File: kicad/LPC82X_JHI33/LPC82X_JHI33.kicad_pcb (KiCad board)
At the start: 2 copper layers, 2 parts

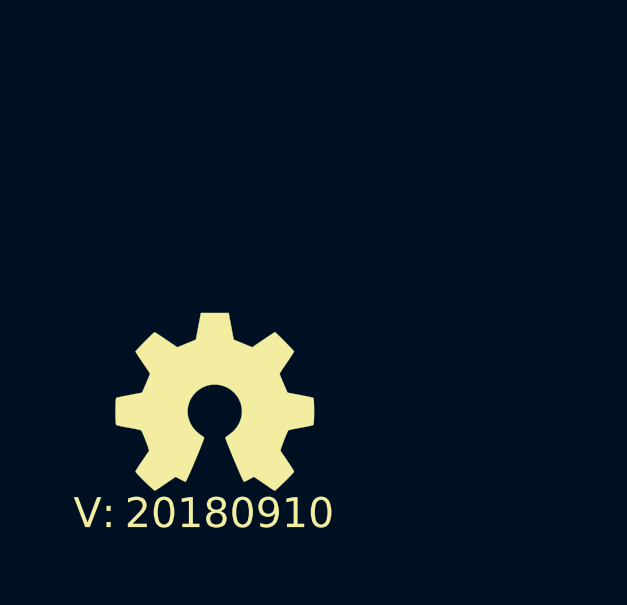
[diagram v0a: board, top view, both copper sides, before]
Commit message: started on LPC824 QFN33 breakout
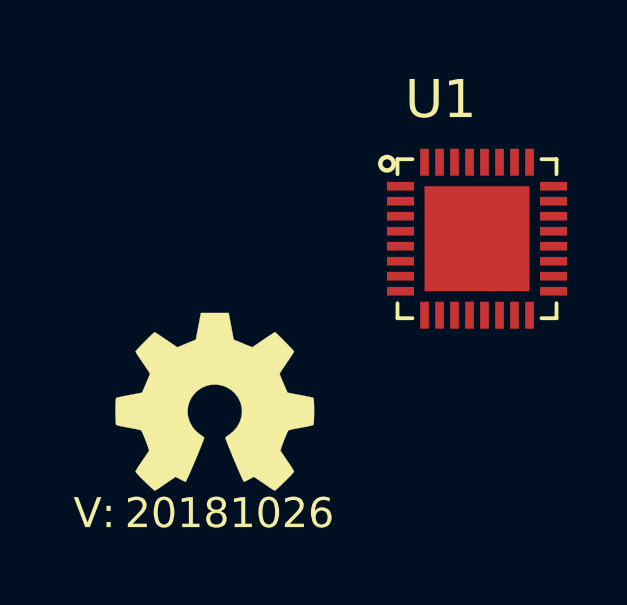
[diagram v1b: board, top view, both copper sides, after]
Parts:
- added U1: LPC824M201JHI33, SquantorIC:SOT617-3, F.Cu at (156.8, 95.5)
- N2: value 20180910 -> 20181026
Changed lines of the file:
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@@
-(kicad_pcb (version 20171130) (host pcbnew 5.0.0-fee4fd1~66~ubuntu18.04.1)
+(kicad_pcb (version 20171130) (host pcbnew 5.0.1-33cea8e~68~ubuntu18.04.1)
   (general
     (thickness 1.6)
@@
     (tracks 0)
     (zones 0)
-    (modules 2)
+    (modules 3)
     (nets 1)
   )
@@
     (pad_drill 0.762)
     (pad_to_mask_clearance 0.2)
+    (solder_mask_min_width 0.25)
     (aux_axis_origin 0 0)
     (visible_elements FFFFFF7F)
@@
       (effects (font (size 1 1) (thickness 0.15)))
     )
-    (fp_text value 20180910 (at -0.4 -0.1) (layer F.SilkS)
+    (fp_text value 20181026 (at -0.4 -0.1) (layer F.SilkS)
       (effects (font (size 1 1) (thickness 0.15)))
     )
@@
     )
   )
+  (module SquantorIC:SOT617-3 (layer F.Cu)
+    (at 156.75 95.55)
+    (descr "<li><b>SOT617-3</b><hr>\n<ul><li>HVQFN32: plastic thermal enhanced very thin quad flat package; no leads; 32 terminals; body 5 x 5 x 0.85 mm\n<li><u>JEDEC</u>: MO-220\n<li><u>IEC</u>: --\n<li><u>JEITA</u>: -- </ul>")
+    (fp_text reference U1 (at -2.4 -3.9) (layer F.SilkS)
+      (effects (font (size 1.27 1.27) (thickness 0.15)) (justify left bottom))
+    )
+    (fp_text value LPC824M201JHI33 (at -4.7 5) (layer F.Fab)
+      (effects (font (size 1.27 1.27) (thickness 0.15)) (justify left bottom))
+    )
+    (fp_line (start -2.025 3.125) (end 2.025 3.125) (layer Dwgs.User) (width 0.127))
+    (fp_line (start 2.025 -3.125) (end -2.025 -3.125) (layer Dwgs.User) (width 0.127))
+    (fp_line (start -3.125 -2.025) (end -3.125 2.025) (layer Dwgs.User) (width 0.127))
+    (fp_line (start -2.65 -2.65) (end -2.025 -2.65) (layer Dwgs.User) (width 0.127))
+    (fp_line (start -2.65 2.65) (end -2.025 2.65) (layer Dwgs.User) (width 0.127))
+    (fp_line (start 2.65 -2.65) (end 2.65 -2.025) (layer Dwgs.User) (width 0.127))
+    (fp_line (start 2.65 2.025) (end 2.65 2.65) (layer Dwgs.User) (width 0.127))
+    (fp_line (start -2.65 -2.65) (end -2.65 -2.025) (layer Dwgs.User) (width 0.127))
+    (fp_line (start -2.65 2.025) (end -2.65 2.65) (layer Dwgs.User) (width 0.127))
+    (fp_line (start -2.025 -3.125) (end -2.025 -2.65) (layer Dwgs.User) (width 0.127))
+    (fp_line (start 2.025 -3.125) (end 2.025 -2.65) (layer Dwgs.User) (width 0.127))
+    (fp_line (start -2.025 3.125) (end -2.025 2.65) (layer Dwgs.User) (width 0.127))
+    (fp_line (start 2.025 3.125) (end 2.025 2.65) (layer Dwgs.User) (width 0.127))
+    (fp_line (start -3.125 -2.025) (end -2.65 -2.025) (layer Dwgs.User) (width 0.127))
+    (fp_line (start 2.65 -2.025) (end 3.125 -2.025) (layer Dwgs.User) (width 0.127))
+    (fp_line (start -3.125 2.025) (end -2.65 2.025) (layer Dwgs.User) (width 0.127))
+    (fp_line (start 2.65 2.025) (end 3.125 2.025) (layer Dwgs.User) (width 0.127))
+    (fp_line (start 2.025 -2.65) (end 2.65 -2.65) (layer Dwgs.User) (width 0.127))
+    (fp_line (start 3.125 -2.025) (end 3.125 2.025) (layer Dwgs.User) (width 0.127))
+    (fp_line (start 2.025 2.65) (end 2.65 2.65) (layer Dwgs.User) (width 0.127))
+    (fp_line (start -2.65 -2.65) (end -2.15 -2.65) (layer F.SilkS) (width 0.127))
+    (fp_line (start -2.65 2.65) (end -2.15 2.65) (layer F.SilkS) (width 0.127))
+    (fp_line (start -2.65 -2.65) (end -2.65 -2.15) (layer F.SilkS) (width 0.127))
+    (fp_line (start -2.65 2.15) (end -2.65 2.65) (layer F.SilkS) (width 0.127))
+    (fp_line (start 2.65 -2.65) (end 2.65 -2.15) (layer F.SilkS) (width 0.127))
+    (fp_line (start 2.65 2.15) (end 2.65 2.65) (layer F.SilkS) (width 0.127))
+    (fp_line (start 2.15 -2.65) (end 2.65 -2.65) (layer F.SilkS) (width 0.127))
+    (fp_line (start 2.15 2.65) (end 2.65 2.65) (layer F.SilkS) (width 0.127))
+    (fp_circle (center -3 -2.5) (end -2.7764 -2.5) (layer F.SilkS) (width 0.15))
+    (fp_poly (pts (xy -0.25 0.25) (xy 0.25 0.25) (xy 0.25 -0.25) (xy -0.25 -0.25)) (layer F.Paste) (width 0))
+    (fp_poly (pts (xy -1.05 0.25) (xy -0.55 0.25) (xy -0.55 -0.25) (xy -1.05 -0.25)) (layer F.Paste) (width 0))
+    (fp_poly (pts (xy 0.55 0.25) (xy 1.05 0.25) (xy 1.05 -0.25) (xy 0.55 -0.25)) (layer F.Paste) (width 0))
+    (fp_poly (pts (xy -0.25 -0.55) (xy 0.25 -0.55) (xy 0.25 -1.05) (xy -0.25 -1.05)) (layer F.Paste) (width 0))
+    (fp_poly (pts (xy -0.25 1.05) (xy 0.25 1.05) (xy 0.25 0.55) (xy -0.25 0.55)) (layer F.Paste) (width 0))
+    (fp_poly (pts (xy 0.55 -0.55) (xy 1.05 -0.55) (xy 1.05 -1.05) (xy 0.55 -1.05)) (layer F.Paste) (width 0))
+    (fp_poly (pts (xy -1.05 -0.55) (xy -0.55 -0.55) (xy -0.55 -1.05) (xy -1.05 -1.05)) (layer F.Paste) (width 0))
+    (fp_poly (pts (xy -1.05 1.05) (xy -0.55 1.05) (xy -0.55 0.55) (xy -1.05 0.55)) (layer F.Paste) (width 0))
+    (fp_poly (pts (xy 0.55 1.05) (xy 1.05 1.05) (xy 1.05 0.55) (xy 0.55 0.55)) (layer F.Paste) (width 0))
+    (pad 28 smd rect (at 0.25 -2.55) (size 0.29 0.9) (layers F.Cu F.Paste F.Mask))
+    (pad 27 smd rect (at 0.75 -2.55) (size 0.29 0.9) (layers F.Cu F.Paste F.Mask))
+    (pad 26 smd rect (at 1.25 -2.55) (size 0.29 0.9) (layers F.Cu F.Paste F.Mask))
+    (pad 25 smd rect (at 1.75 -2.55) (size 0.29 0.9) (layers F.Cu F.Paste F.Mask))
+    (pad 29 smd rect (at -0.25 -2.55) (size 0.29 0.9) (layers F.Cu F.Paste F.Mask))
+    (pad 30 smd rect (at -0.75 -2.55) (size 0.29 0.9) (layers F.Cu F.Paste F.Mask))
+    (pad 31 smd rect (at -1.25 -2.55) (size 0.29 0.9) (layers F.Cu F.Paste F.Mask))
+    (pad 32 smd rect (at -1.75 -2.55) (size 0.29 0.9) (layers F.Cu F.Paste F.Mask))
+    (pad 12 smd rect (at -0.25 2.55 180) (size 0.29 0.9) (layers F.Cu F.Paste F.Mask))
+    (pad 11 smd rect (at -0.75 2.55 180) (size 0.29 0.9) (layers F.Cu F.Paste F.Mask))
+    (pad 10 smd rect (at -1.25 2.55 180) (size 0.29 0.9) (layers F.Cu F.Paste F.Mask))
+    (pad 9 smd rect (at -1.75 2.55 180) (size 0.29 0.9) (layers F.Cu F.Paste F.Mask))
+    (pad 13 smd rect (at 0.25 2.55 180) (size 0.29 0.9) (layers F.Cu F.Paste F.Mask))
+    (pad 14 smd rect (at 0.75 2.55 180) (size 0.29 0.9) (layers F.Cu F.Paste F.Mask))
+    (pad 15 smd rect (at 1.25 2.55 180) (size 0.29 0.9) (layers F.Cu F.Paste F.Mask))
+    (pad 16 smd rect (at 1.75 2.55 180) (size 0.29 0.9) (layers F.Cu F.Paste F.Mask))
+    (pad 20 smd rect (at 2.55 0.25 270) (size 0.29 0.9) (layers F.Cu F.Paste F.Mask))
+    (pad 19 smd rect (at 2.55 0.75 270) (size 0.29 0.9) (layers F.Cu F.Paste F.Mask))
+    (pad 18 smd rect (at 2.55 1.25 90) (size 0.29 0.9) (layers F.Cu F.Paste F.Mask))
+    (pad 17 smd rect (at 2.55 1.75 270) (size 0.29 0.9) (layers F.Cu F.Paste F.Mask))
+    (pad 21 smd rect (at 2.55 -0.25 270) (size 0.29 0.9) (layers F.Cu F.Paste F.Mask))
+    (pad 22 smd rect (at 2.55 -0.75 270) (size 0.29 0.9) (layers F.Cu F.Paste F.Mask))
+    (pad 23 smd rect (at 2.55 -1.25 270) (size 0.29 0.9) (layers F.Cu F.Paste F.Mask))
+    (pad 24 smd rect (at 2.55 -1.75 270) (size 0.29 0.9) (layers F.Cu F.Paste F.Mask))
+    (pad 4 smd rect (at -2.55 -0.25 90) (size 0.29 0.9) (layers F.Cu F.Paste F.Mask))
+    (pad 3 smd rect (at -2.55 -0.75 90) (size 0.29 0.9) (layers F.Cu F.Paste F.Mask))
+    (pad 2 smd rect (at -2.55 -1.25 270) (size 0.29 0.9) (layers F.Cu F.Paste F.Mask))
+    (pad 1 smd rect (at -2.55 -1.75 90) (size 0.29 0.9) (layers F.Cu F.Paste F.Mask))
+    (pad 5 smd rect (at -2.55 0.25 90) (size 0.29 0.9) (layers F.Cu F.Paste F.Mask))
+    (pad 6 smd rect (at -2.55 0.75 90) (size 0.29 0.9) (layers F.Cu F.Paste F.Mask))
+    (pad 7 smd rect (at -2.55 1.25 90) (size 0.29 0.9) (layers F.Cu F.Paste F.Mask))
+    (pad 8 smd rect (at -2.55 1.75 90) (size 0.29 0.9) (layers F.Cu F.Paste F.Mask))
+    (pad 33 smd rect (at 0 0) (size 3.5 3.5) (layers F.Cu F.Paste F.Mask))
+  )
 )

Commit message: further pcb placement
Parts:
- added C1: 18p, SquantorRcl:C_0402, F.Cu at (87.4, 114.4)
- added C2: 1u, SquantorRcl:C_0603, F.Cu at (88.2, 112.5)
- added C3: 1u, SquantorRcl:C_0603, F.Cu at (91.1, 112.5)
- added C4: 18p, SquantorRcl:C_0402, F.Cu at (85.1, 117.7)
- added C5: 100n, SquantorRcl:C_0402, F.Cu at (87.9, 111.1)
- added C6: 100n, SquantorRcl:C_0402, F.Cu at (90.2, 111.1)
- added FB1: Ferrite_Bead_Small, SquantorRcl:C_0402, F.Cu at (88.5, 114.4)
- added FB2: Ferrite_Bead_Small, SquantorRcl:C_0402, F.Cu at (91.3, 114.5)
- added FB3: Ferrite_Bead_Small, SquantorRcl:C_0402, F.Cu at (89.9, 114.4)
- added J1: Conn_02x09_Odd_Even, SquantorConnectors:Header-0254-2X09-H010, F.Cu at (78.7, 106.7)
- added J2: Conn_02x09_Odd_Even, SquantorConnectors:Header-0254-2X09-H010, F.Cu at (99.1, 106.7)
- added J3: JTAG_2X05, SquantorConnectors:Header-0127-2X05-H006, F.Cu at (91.9, 96.8)
- added R1: 100, SquantorRcl:R_0402_hand, F.Cu at (94.6, 99.1)
- added R2: 100, SquantorRcl:R_0402_hand, F.Cu at (92.2, 99.1)
- added R3: 100, SquantorRcl:R_0402_hand, F.Cu at (90.2, 99.7)
- added R4: 47K, SquantorRcl:R_0402_hand, F.Cu at (88.8, 99.7)
- added R5: 47K, SquantorRcl:R_0402_hand, F.Cu at (84.7, 101.6)
- added R6: 100k, SquantorRcl:R_0402_hand, F.Cu at (94.6, 100.4)
- added R7: 100k, SquantorRcl:R_0402_hand, F.Cu at (92.2, 100.4)
- added S1: 2pin_tact_switch, SquantorButtons:TD-85XU, F.Cu at (86.3, 98.3)
- added S2: 2pin_tact_switch, SquantorButtons:TD-85XU, F.Cu at (83.0, 98.3)
- added SJ1: SolderJumper_3way_1conn, SquantorSpecial:solder_jumper_3way_12conn, F.Cu at (85.7, 111.2)
- added SJ2: SolderJumper_3way_1conn, SquantorSpecial:solder_jumper_3way_12conn, F.Cu at (84.3, 111.2)
- added Y1: 12MHz, SquantorCrystal:Crystal_3225_4, F.Cu at (85.0, 115.0)
- N1, N2: moved to B.Cu
- moved U1 68.8 mm to (88.9, 106.7), turned to 270 degrees
- moved N2 59.8 mm to (90.4, 117.2), turned to 180 degrees
- moved N1 58.0 mm to (91.3, 113.4), turned to 180 degrees
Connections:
- U1 pad 1: (no net) -> /PIO0_13
- U1 pad 10: (no net) -> /PIO0_16
- U1 pad 11: (no net) -> /PIO0_27
- U1 pad 12: (no net) -> /PIO0_26
- U1 pad 13: (no net) -> /PIO0_25
- U1 pad 14: (no net) -> /PIO0_24
- U1 pad 15: (no net) -> /PIO0_15
- U1 pad 16: (no net) -> /PIO0_1
- U1 pad 17: (no net) -> /PIO0_9-XTALOUT
- U1 pad 18: (no net) -> /PIO0_8-XTALIN
- U1 pad 19: (no net) -> Net-(C2-Pad1)
- U1 pad 2: (no net) -> /PIO0_12
- U1 pad 20: (no net) -> Net-(C3-Pad2)
- U1 pad 21: (no net) -> Net-(C3-Pad1)
- U1 pad 22: (no net) -> /PIO0_7
- U1 pad 23: (no net) -> /PIO0_6
- U1 pad 24: (no net) -> /PIO0_0
- U1 pad 25: (no net) -> /PIO0_14
- U1 pad 26: (no net) -> /PIO0_23
- U1 pad 27: (no net) -> /PIO0_22
- U1 pad 28: (no net) -> /PIO0_21
- U1 pad 29: (no net) -> /PIO0_20
- U1 pad 3: (no net) -> /RESET
- U1 pad 30: (no net) -> /PIO0_19
- U1 pad 31: (no net) -> /PIO0_18
- U1 pad 32: (no net) -> /PIO0_17
- U1 pad 33: (no net) -> VSS
- U1 pad 4: (no net) -> /PIO0_4
- U1 pad 5: (no net) -> /PIO0_28
- U1 pad 6: (no net) -> /PIO0_3
- U1 pad 7: (no net) -> /PIO0_2
- U1 pad 8: (no net) -> /PIO0_11
- U1 pad 9: (no net) -> /PIO0_10
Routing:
- added copper zone on In2.Cu, net VDD
- added copper zone on In1.Cu, net VSS
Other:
- board outline added: 26 x 23.5 mm
- copper layers 2 -> 4
- net class Default: clearance 0.1524 -> 0.127; trace_width 0.1524 -> 0.127; via_dia 0.381 -> 0.3556
- rule pad_to_mask_clearance: 0.2 -> 0.1
- rule solder_mask_min_width: 0.25 -> 0.2
- rule trace_clearance: 0.1524 -> 0.127
- rule trace_min: 0.1524 -> 0.127
- rule via_min_size: 0.381 -> 0.3556

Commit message: started with first layout
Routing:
- net /PIO0_2: track 0.00 -> 23.4 mm, vias 0 -> 2
- net /PIO0_3: track 0.00 -> 18.4 mm, vias 0 -> 2
- net /PIO0_28: track 0.00 -> 17.6 mm
- net /PIO0_15: track 0.00 -> 10.5 mm
- net /PIO0_10: track 0.00 -> 10.2 mm
- net /PIO0_25: track 0.00 -> 9.85 mm
- net /PIO0_27: track 0.00 -> 9.55 mm
- net /PIO0_11: track 0.00 -> 8.25 mm
- net /RESET: track 0.00 -> 8.24 mm
- net /PIO0_1: track 0.00 -> 7.74 mm
- net /PIO0_24: track 0.00 -> 7.11 mm
- net /PIO0_16: track 0.00 -> 6.87 mm
- net /PIO0_26: track 0.00 -> 6.47 mm
- net VSS: track 0.00 -> 4.49 mm, vias 0 -> 2
- net VDD: track 0.00 -> 3.83 mm, vias 0 -> 3
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
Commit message: finished routing tracks
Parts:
- moved FB2 0.30 mm to (91.0, 114.5)
- moved FB3 0.14 mm to (89.8, 114.5)
- moved FB1 0.14 mm to (88.6, 114.5)
- moved C5 0.10 mm to (87.9, 111.2)
- moved C6 0.10 mm to (90.2, 111.2)
- moved C1 0.10 mm to (87.4, 114.5)
- moved C2 0.10 mm to (88.2, 112.6)
- moved C3 0.10 mm to (91.1, 112.6)
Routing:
- net /PIO0_12: track 1.80 -> 21.6 mm, vias 0 -> 2
- net /PIO0_7: track 0.00 -> 14.1 mm
- net /PIO0_4: track 0.00 -> 13.0 mm, vias 0 -> 2
- net /PIO0_0: track 0.00 -> 11.8 mm
- net /PIO0_23: track 0.00 -> 10.5 mm
- net /PIO0_17: track 0.00 -> 10.3 mm
- net /PIO0_6: track 0.00 -> 9.99 mm
- net /PIO0_21: track 0.00 -> 9.81 mm
- net /PIO0_19: track 0.00 -> 9.64 mm
- net VSS: track 4.49 -> 13.9 mm, vias 2 -> 7
- net /PIO0_13: track 0.00 -> 8.76 mm
- net /PIO0_9: track 0.00 -> 8.57 mm
- net /PIO0_8: track 0.00 -> 7.90 mm
- net /PIO0_14: track 0.00 -> 7.74 mm
- net /XTALOUT: track 0.00 -> 7.29 mm
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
